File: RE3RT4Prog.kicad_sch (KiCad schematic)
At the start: 71 parts, among them J1 Conn_01x08, J2 Conn_01x08, J3 DE9_Receptacle_MountingHoles, J4 +5V, J5 GND, J6 PicKit, J7 Barrel_Jack_MountingPin, Q1 BD140, Q2 2N7000, Q3 2N7000, Q4 2N7000, U1 DG408, U2 155RE3, U3 556RT4, U4 74HC164, U6 PIC18F26K22-xSP, U7 MAX232, Y1 7.3728

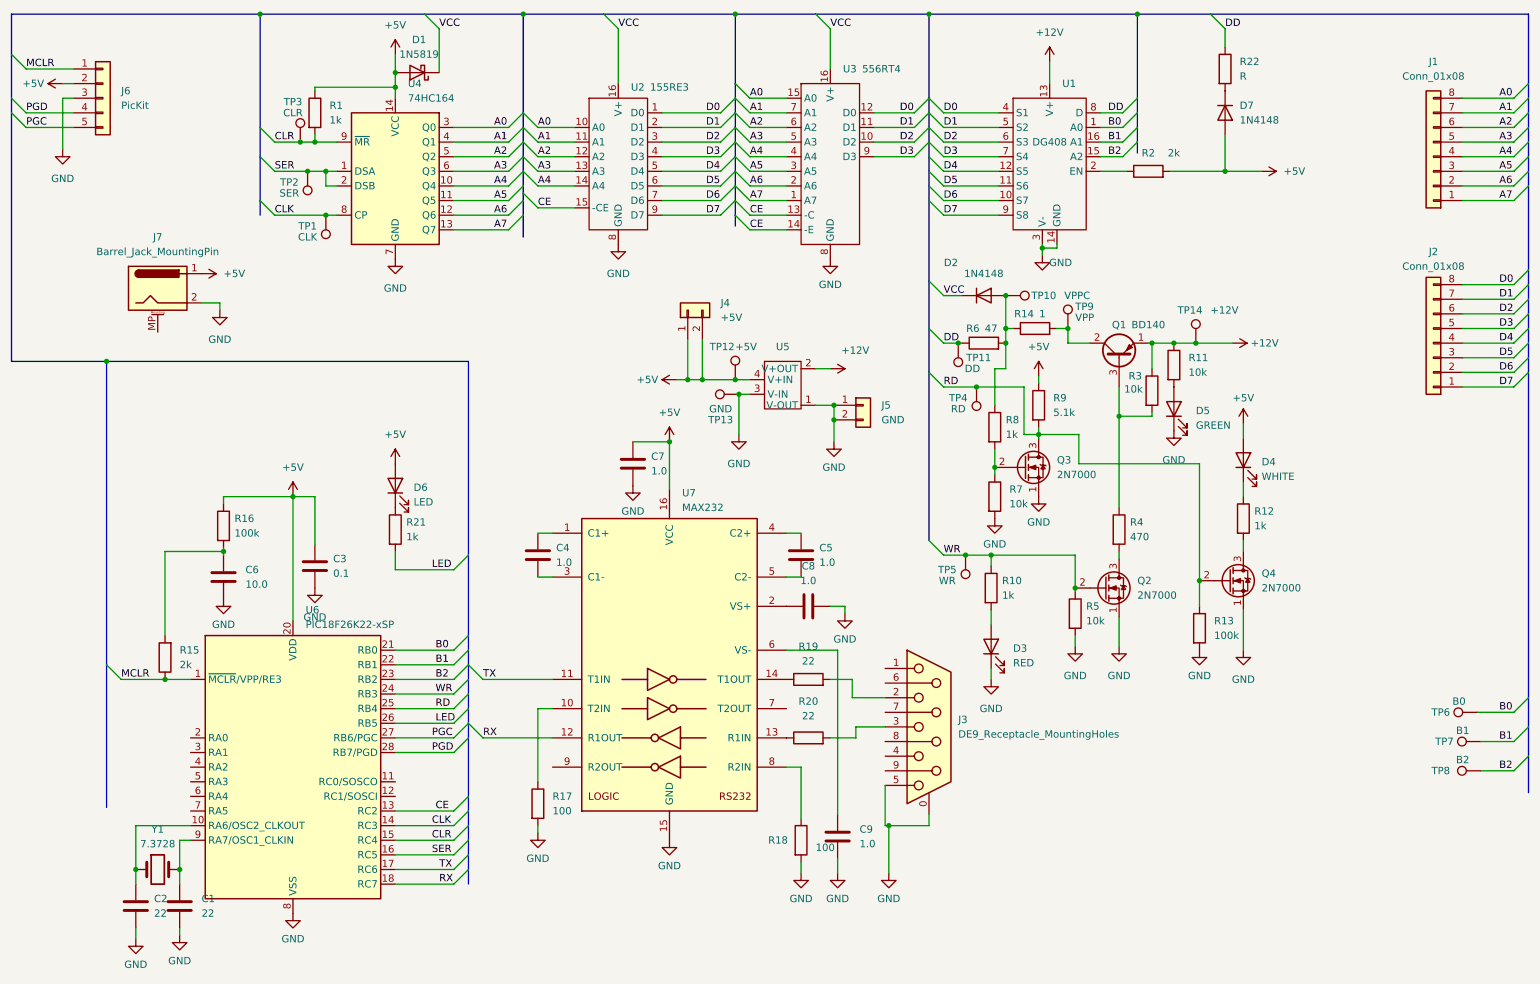
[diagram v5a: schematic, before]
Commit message: Added AVRISP connector
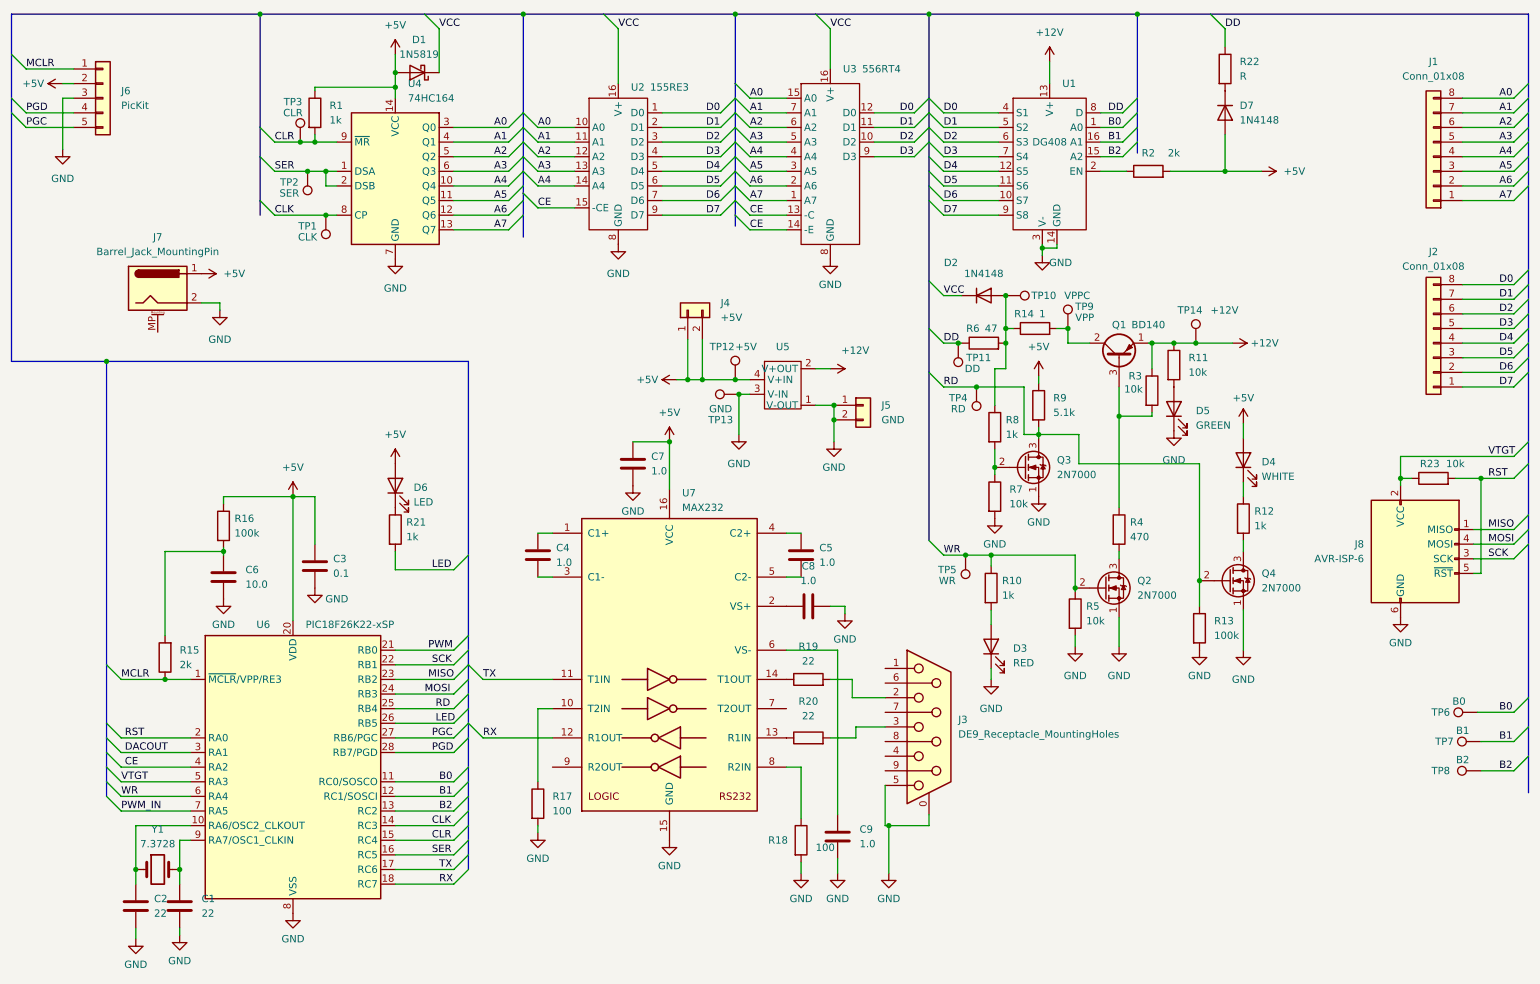
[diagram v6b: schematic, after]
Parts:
- added J8: AVR-ISP-6, Connector_IDC:IDC-Header_2x03_P2.54mm_Vertical, symbol Connector:AVR-ISP-6
- added R23: 10k, symbol Device:R
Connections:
- net B0: now also U6.11 (RC0/SOSCO); no longer U6.21 (RB0)
- net B1: now also U6.12 (RC1/SOSCI); no longer U6.22 (RB1)
- net B2: now also U6.13 (RC2); no longer U6.23 (RB2)
- net CE: now also U6.4 (RA2); no longer U6.13 (RC2)
- net GND: now also J8.6 (GND)
- net WR: now also U6.6 (RA4); no longer U6.24 (RB3)
- net RST: now reaches U6.2 (RA0)
- net RST: now also J8.5 (~{RST}), R23.2
- net DACOUT: now reaches U6.3 (RA1)
- net VTGT: now reaches U6.5 (RA3)
- net VTGT: now also J8.2 (VCC), R23.1
- net PWM_IN: now reaches U6.7 (RA5)
- new net MISO: J8.1 (MISO), U6.23 (RB2)
- new net MOSI: J8.4 (MOSI), U6.24 (RB3)
- new net PWM: U6.21 (RB0)
- new net SCK: J8.3 (SCK), U6.22 (RB1)
